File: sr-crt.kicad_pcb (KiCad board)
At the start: 4 copper layers, 38.5 x 33.2 mm, 20 parts, among them J1 Conn_02x03_Odd_Even, J2 Barrel_Jack_MountingPin, J3 DIN-6, U1 SN65LVDS2DBV, U2 SN65LVDS2DBV, U3 ADuM1200BR

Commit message: Added bits to silkscreen
As above
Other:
- board text added: "Copyright © 2025 SRB Computer Co."
- board text added: "SR-CRT"
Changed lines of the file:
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@@
 		(tags "resistor")
 		(property "Reference" "R2"
-			(at -2.25 0.25 270)
+			(at 0 1.5 0)
 			(layer "F.SilkS")
 			(effects
@@
 		(tags "Through hole vertical IDC box header THT 2x03 2.54mm double row")
 		(property "Reference" "J1"
-			(at -1.96 11.58 0)
+			(at 7.24 10.05 0)
 			(layer "F.SilkS")
 			(effects
@@
 		(tags "capacitor")
 		(property "Reference" "C7"
-			(at 2.475 -1 270)
+			(at 0.725 -1.45 270)
 			(layer "F.SilkS")
 			(effects
@@
 		)
 	)
+	(gr_curve
+		(pts
+			(xy 63.75 33.9) (xy 60.75 34.15) (xy 57.75 33.9) (xy 57.75 33.9)
+		)
+		(stroke
+			(width 0.1)
+			(type default)
+		)
+		(layer "F.SilkS")
+	)
+	(gr_curve
+		(pts
+			(xy 57.75 30.65) (xy 57.5 32.4) (xy 57.75 33.9) (xy 57.75 33.9)
+		)
+		(stroke
+			(width 0.1)
+			(type default)
+		)
+		(layer "F.SilkS")
+	)
+	(gr_poly
+		(pts
+			(xy 57.5 30.4) (xy 57.7 30.65) (xy 57.6 32.15) (xy 57.7 33.9) (xy 57.5 34.15)
+		)
+		(stroke
+			(width 0.1)
+			(type solid)
+		)
+		(fill yes)
+		(layer "F.SilkS")
+	)
+	(gr_line
+		(start 64 34.15)
+		(end 64 30.4)
+		(stroke
+			(width 0.1)
+			(type default)
+		)
+		(layer "F.SilkS")
+	)
+	(gr_curve
+		(pts
+			(xy 63.75 30.65) (xy 64 32.4) (xy 63.75 33.9) (xy 63.75 33.9)
+		)
+		(stroke
+			(width 0.1)
+			(type default)
+		)
+		(layer "F.SilkS")
+	)
+	(gr_line
+		(start 64 34.15)
+		(end 57.5 34.15)
+		(stroke
+			(width 0.1)
+			(type default)
+		)
+		(layer "F.SilkS")
+	)
+	(gr_poly
+		(pts
+			(xy 57.5 34.15) (xy 64 34.15) (xy 63.75 33.95) (xy 60.75 34.05) (xy 57.75 33.95)
+		)
+		(stroke
+			(width 0.1)
+			(type solid)
+		)
+		(fill yes)
+		(layer "F.SilkS")
+	)
+	(gr_poly
+		(pts
+			(xy 64 30.4) (xy 63.8 30.65) (xy 63.95 32.325) (xy 63.8 33.9) (xy 64 34.15)
+		)
+		(stroke
+			(width 0.1)
+			(type solid)
+		)
+		(fill yes)
+		(layer "F.SilkS")
+	)
+	(gr_line
+		(start 64 30.4)
+		(end 57.5 30.4)
+		(stroke
+			(width 0.1)
+			(type default)
+		)
+		(layer "F.SilkS")
+	)
+	(gr_line
+		(start 57.5 30.4)
+		(end 57.5 34.15)
+		(stroke
+			(width 0.1)
+			(type default)
+		)
+		(layer "F.SilkS")
+	)
+	(gr_curve
+		(pts
+			(xy 57.75 30.65) (xy 61 30.4) (xy 63.75 30.65) (xy 63.75 30.65)
+		)
+		(stroke
+			(width 0.1)
+			(type default)
+		)
+		(layer "F.SilkS")
+	)
+	(gr_poly
+		(pts
+			(xy 57.5 30.4) (xy 64 30.4) (xy 63.8 30.6) (xy 60.75 30.45) (xy 57.75 30.6)
+		)
+		(stroke
+			(width 0.1)
+			(type solid)
+		)
+		(fill yes)
+		(layer "F.SilkS")
+	)
 	(gr_arc
 		(start 82.25 57.25)
@@
 		(layer "Edge.Cuts")
 	)
+	(gr_text "SR-CRT"
+		(at 57.65 32.9 0)
+		(layer "F.SilkS")
+		(effects
+			(font
+				(size 1 1)
+				(thickness 0.2)
+				(bold yes)
+			)
+			(justify left bottom)
+		)
+	)
+	(gr_text "Copyright © 2025 SRB Computer Co."
+		(at 44.15 48.75 0)
+		(layer "F.SilkS")
+		(effects
+			(font
+				(size 0.65 0.65)
+				(thickness 0.1)
+			)
+			(justify left bottom)
+		)
+	)
+	(dimension
+		(type orthogonal)
+		(layer "User.1")
+		(pts
+			(xy 79.7322 24.25) (xy 79.75 57.5)
+		)
+		(height 8.5178)
+		(orientation 1)
+		(format
+			(prefix "")
+			(suffix "")
+			(units 3)
+			(units_format 0)
+			(precision 4)
+			(suppress_zeroes yes)
+		)
+		(style
+			(thickness 0.1)
+			(arrow_length 1.27)
+			(text_position_mode 0)
+			(arrow_direction outward)
+			(extension_height 0.58642)
+			(extension_offset 0.5)
+			(keep_text_aligned yes)
+		)
+		(gr_text "33.25"
+			(at 87.1 40.875 90)
+			(layer "User.1")
+			(effects
+				(font
+					(size 1 1)
+					(thickness 0.15)
+				)
+			)
+		)
+	)
+	(dimension
+		(type orthogonal)
+		(layer "User.1")
+		(pts
+			(xy 43.75 27) (xy 82.25 27)
+		)
+		(height -9.5)
+		(orientation 0)
+		(format
+			(prefix "")
+			(suffix "")
+			(units 3)
+			(units_format 0)
+			(precision 4)
+			(suppress_zeroes yes)
+		)
+		(style
+			(thickness 0.1)
+			(arrow_length 1.27)
+			(text_position_mode 0)
+			(arrow_direction outward)
+			(extension_height 0.58642)
+			(extension_offset 0.5)
+			(keep_text_aligned yes)
+		)
+		(gr_text "38.5"
+			(at 63 16.35 0)
+			(layer "User.1")
+			(effects
+				(font
+					(size 1 1)
+					(thickness 0.15)
+				)
+			)
+		)
+	)
 	(via

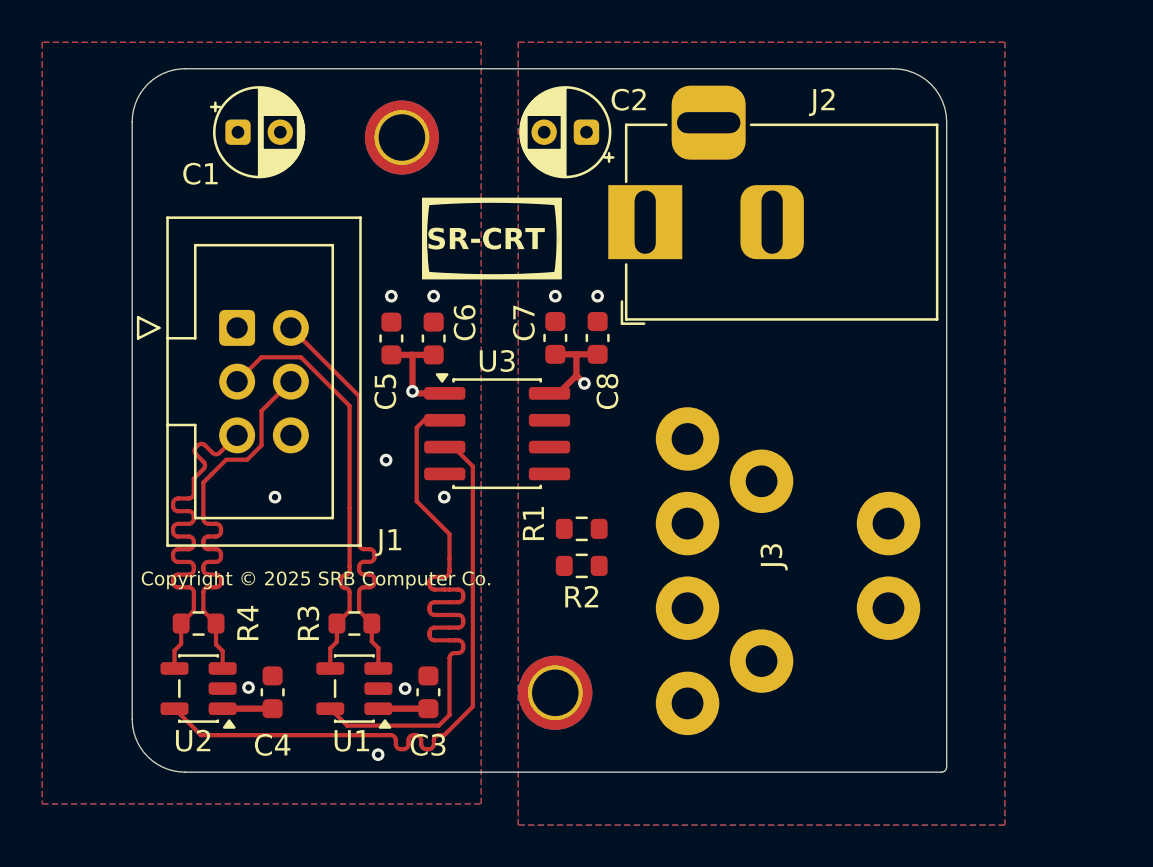
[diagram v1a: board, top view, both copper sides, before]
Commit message: Sent to manufacturing
Specifically sr-crt-2.zip
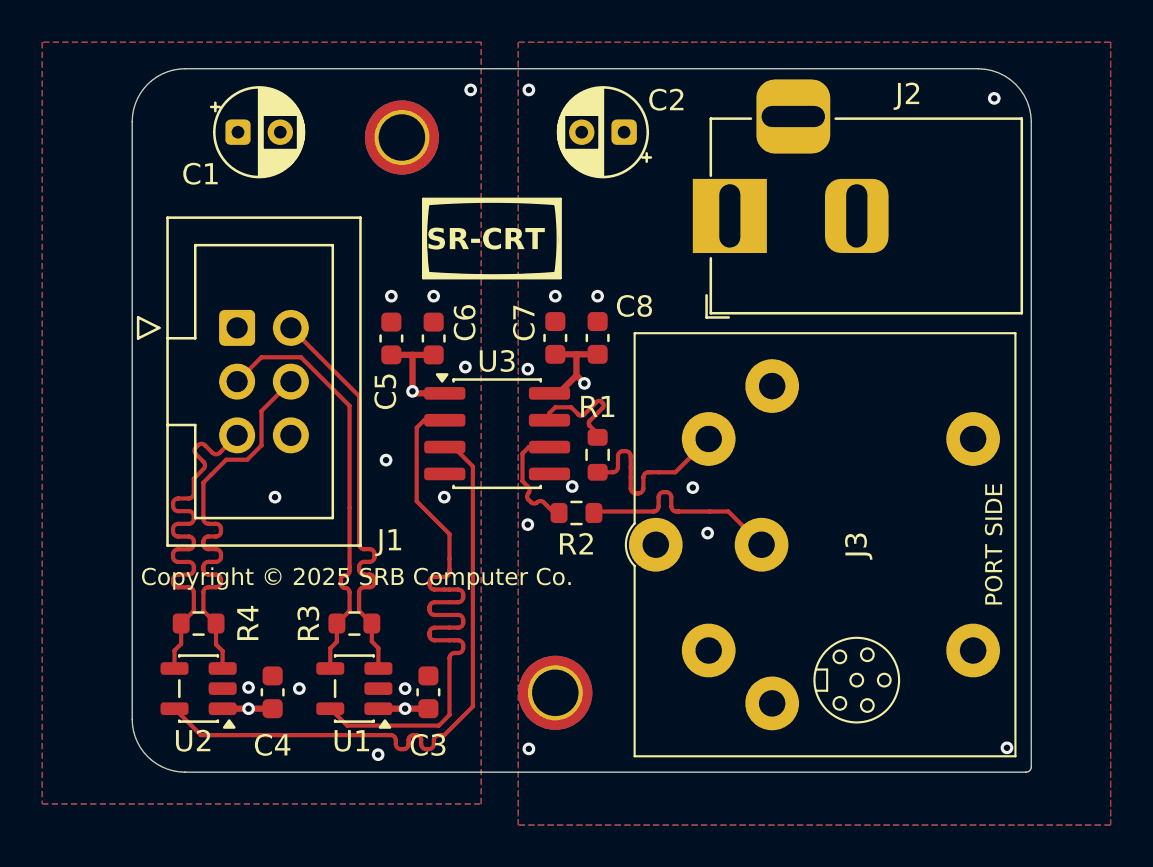
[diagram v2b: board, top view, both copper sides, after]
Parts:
- moved J3 4.03 mm to (78.5, 46.8)
- moved J2 4.01 mm to (72.0, 31.2)
- moved R1 3.58 mm to (65.8, 42.5), turned to -90 degrees
- moved R2 2.51 mm to (64.8, 45.2)
- moved C2 1.78 mm to (67.0, 27.2)
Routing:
- net Net-(J3-Pad6): track 0.00 -> 9.98 mm
- net Net-(J3-Pad4): track 0.00 -> 9.23 mm
- net /SYNC_TTL: track 0.00 -> 5.51 mm
- net /PIXEL_TTL: track 0.00 -> 5.50 mm
- net VDD3_3: vias 1 -> 3
- net GND5: vias 2 -> 11
- net GND3_3: vias 8 -> 11
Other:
- board size 38.5 x 33.2 mm -> 42.5 x 33.2 mm

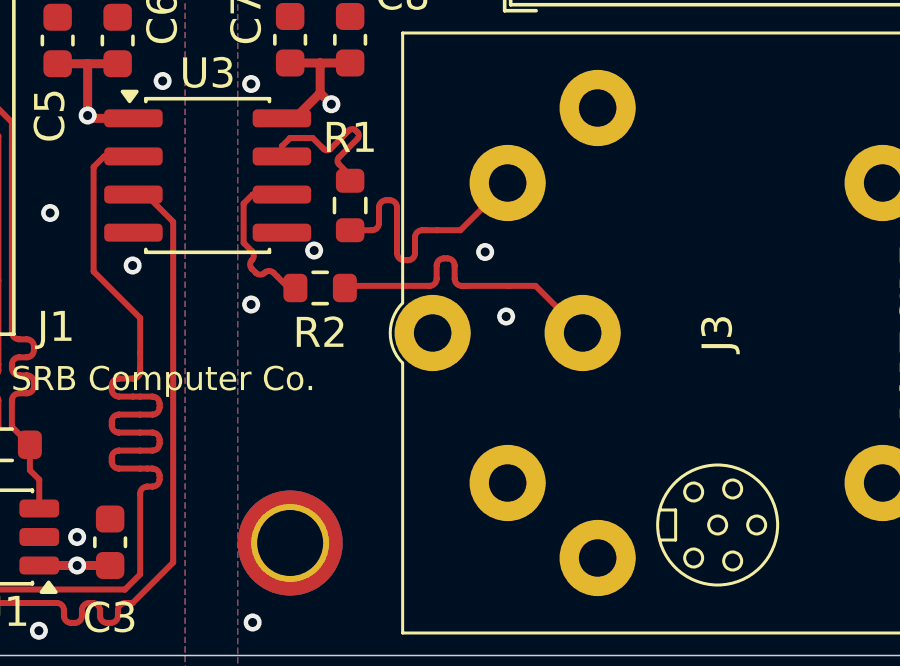
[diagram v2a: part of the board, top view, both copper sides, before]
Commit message: Updated PCB
Fixed pin issues
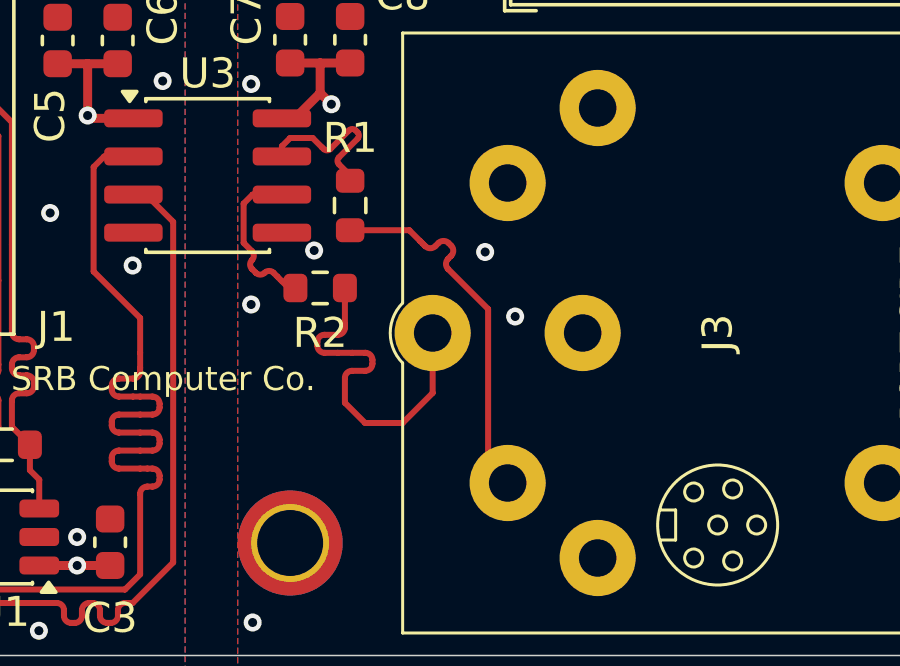
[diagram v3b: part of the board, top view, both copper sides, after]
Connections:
- J3 pad 2: unconnected-(J3-Pad2) -> Net-(J3-Pad2)
- J3 pad 3: unconnected-(J3-Pad3) -> Net-(J3-Pad3)
- J3 pad 4: Net-(J3-Pad4) -> unconnected-(J3-Pad4)
- J3 pad 6: Net-(J3-Pad6) -> unconnected-(J3-Pad6)
- J3 pad 7: GND5 -> (no net)
- R1 pad 2: Net-(J3-Pad4) -> Net-(J3-Pad2)
- R2 pad 2: Net-(J3-Pad6) -> Net-(J3-Pad3)
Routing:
- net Net-(J3-Pad2): track 0.00 -> 12.6 mm
- net Net-(J3-Pad3): track 0.00 -> 12.4 mm
- net Net-(J3-Pad6): track 9.98 -> 0.00 mm
- net Net-(J3-Pad4): track 9.23 -> 0.00 mm
